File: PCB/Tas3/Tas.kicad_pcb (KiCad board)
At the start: 2 copper layers, 70 x 70 mm, 27 parts, among them J1 Shelly 1, J2 Conn_01x07, J3 USB-C, U1 MD8942, U2 Barcode, U3 CH340X, U4 ISL89410

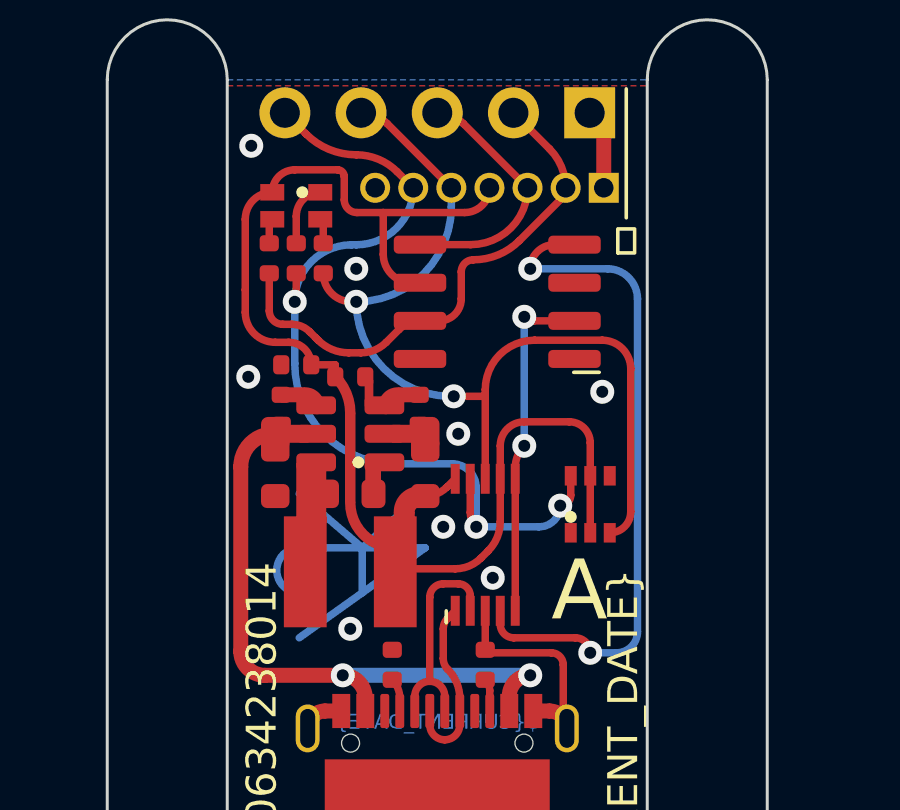
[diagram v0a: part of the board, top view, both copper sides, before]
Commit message: Fix output driver
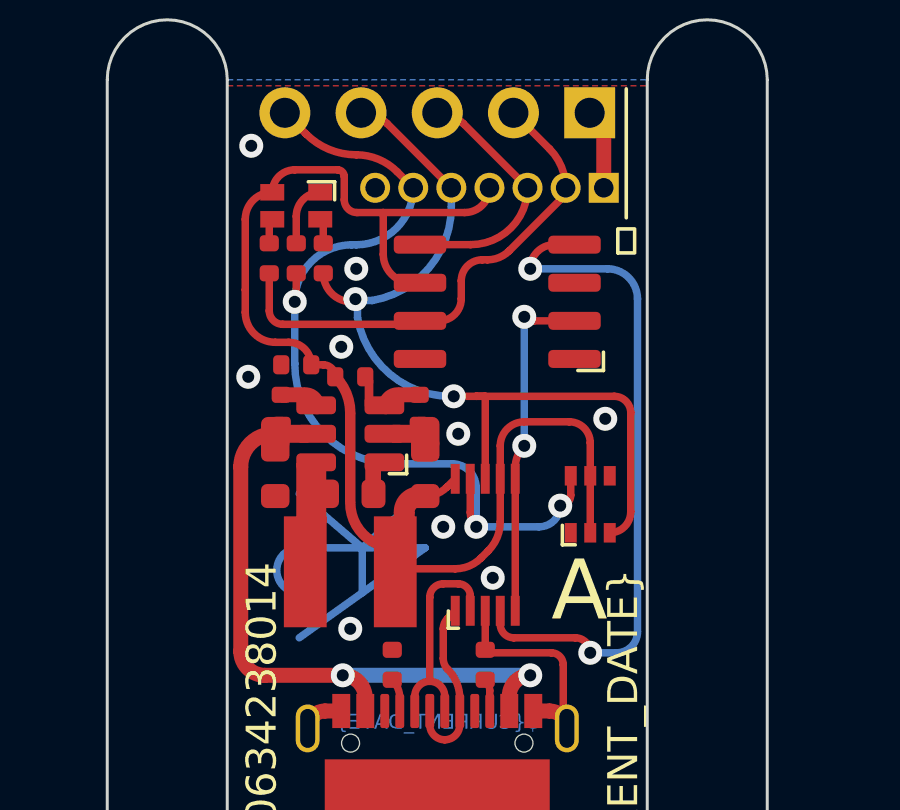
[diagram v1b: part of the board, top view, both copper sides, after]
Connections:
- U4 pad 1: unconnected-(U4-NC-Pad1) -> GND
- U4 pad 8: unconnected-(U4-NC-Pad8) -> GND
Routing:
- net G: track 32.1 -> 29.9 mm
- net B: track 17.0 -> 16.3 mm
- net GND: vias 8 -> 9

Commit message: As ordered
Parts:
- added U5: ZXGD3009E6, RevK:SOT-23-6, F.Cu at (103.4, 48.1)
- U4: value ISL89410 -> ZXGD3009E6; footprint RevK:SO-8_3.9x4.9mm_P1.27mm -> RevK:SOT-23-6
- moved U4 1.92 mm to (99.1, 48.1)
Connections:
- U4 pad 1: GND -> +3V3
- U4 pad 4: RST -> B
- U4 pad 5: RST+ -> unconnected-(U4-NC-Pad5)
- U4 pad 6: +3V3 -> B
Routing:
- net GND: track 10.8 -> 16.1 mm
- net RST+: track 8.58 -> 11.7 mm
- net +3V3: track 35.3 -> 38.2 mm
- net RST: track 22.3 -> 19.8 mm
- net B: track 16.3 -> 18.8 mm, vias 0 -> 1
- net GPIO0: track 11.2 -> 12.4 mm
- net G: track 29.9 -> 29.3 mm
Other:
- board text removed: "${TITLE}"
- board text removed: "This is an assembled printed circuit board. This is a component, with no case or leads. Snap off any extra blank panels. Use this part for your own projects as you wish. Made in China for Andrews & Arnold Ltd."
- board text removed: "®"

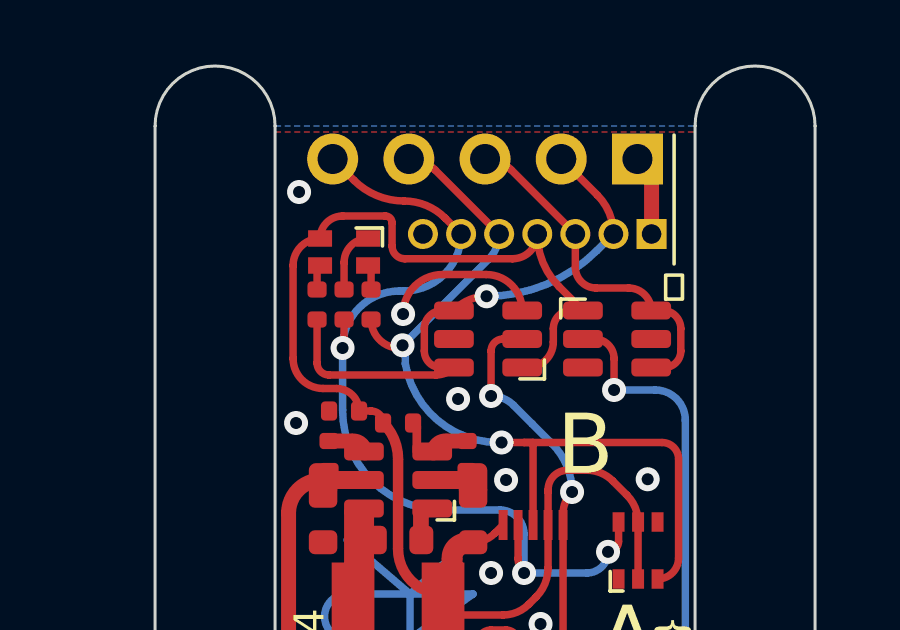
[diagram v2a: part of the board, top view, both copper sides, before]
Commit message: GPIO buffer
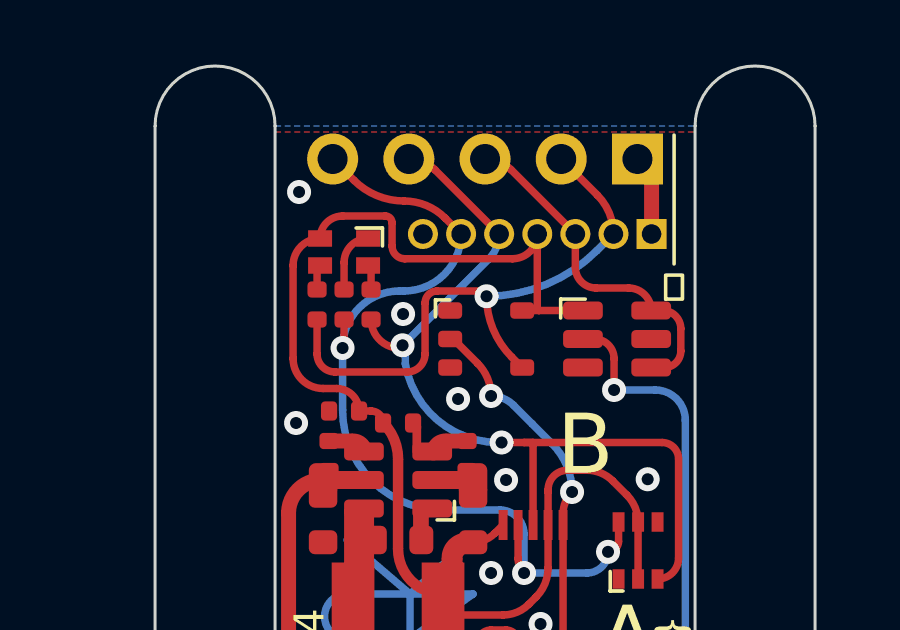
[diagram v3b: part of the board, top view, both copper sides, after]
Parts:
- removed U4: ZXGD3009E6, RevK:SOT-23-6
- added U6: 74LVC1G17W5-7, RevK:SOT-25, F.Cu at (99.0, 48.1)
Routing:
- net GND: track 16.1 -> 10.8 mm
- net +3V3: track 38.2 -> 36.5 mm
- net B: track 18.8 -> 20.1 mm

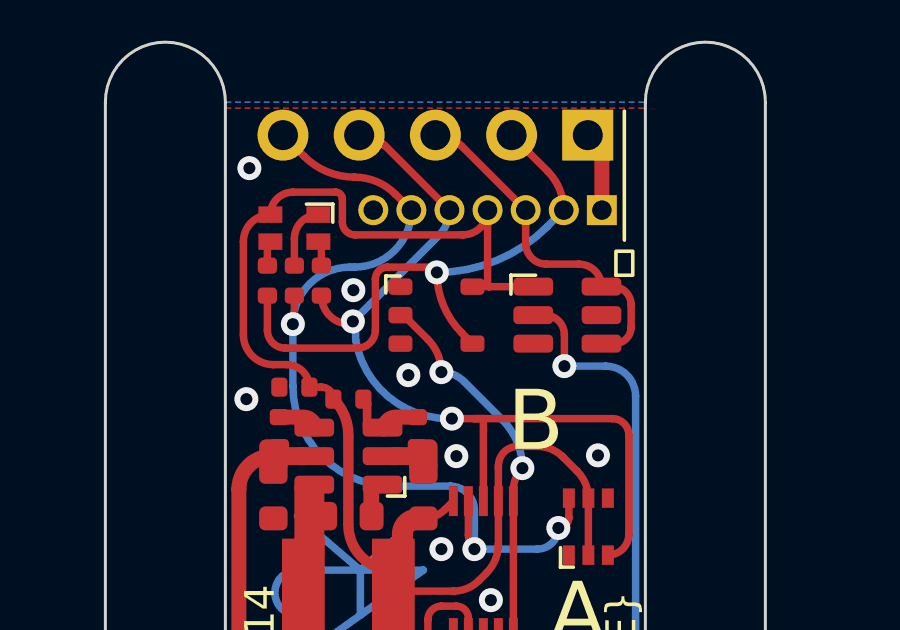
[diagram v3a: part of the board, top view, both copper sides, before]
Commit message: Put back, as does not seem to save much
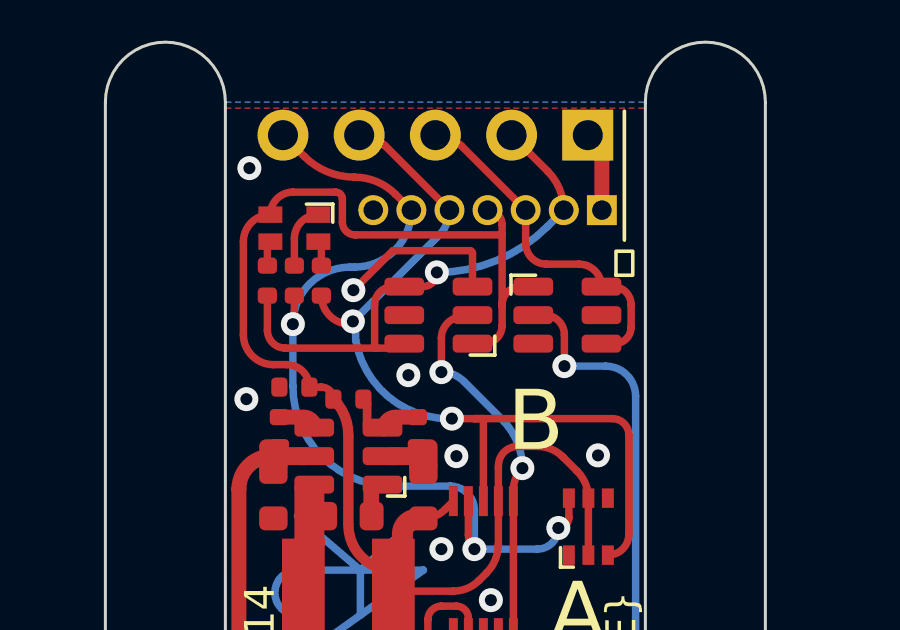
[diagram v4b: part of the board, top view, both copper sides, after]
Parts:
- removed U6: 74LVC1G17W5-7, RevK:SOT-25
- added U4: ZXGD3009E6, RevK:SOT-23-6, F.Cu at (99.1, 48.1)
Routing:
- net GND: track 10.8 -> 16.5 mm
- net B: track 20.1 -> 17.6 mm
- net +3V3: track 36.5 -> 37.9 mm
- net RST+: track 11.7 -> 10.9 mm

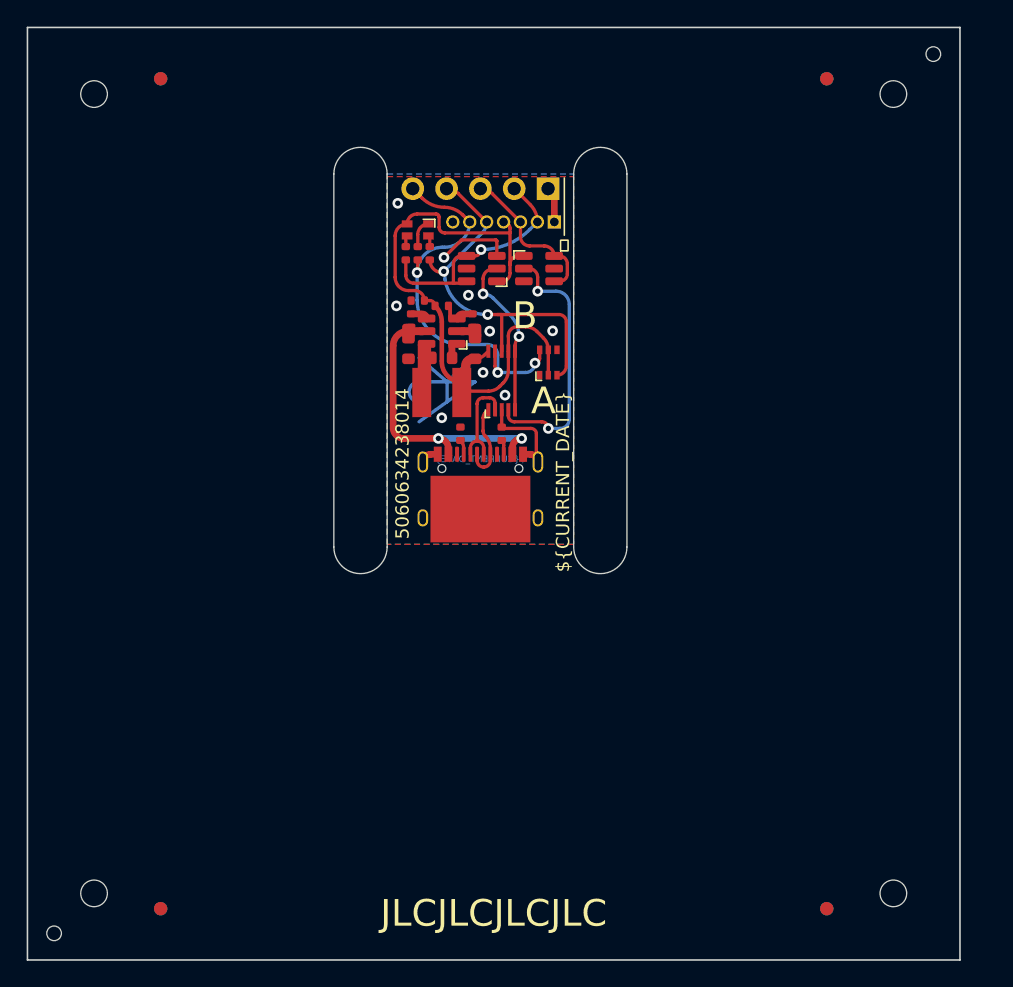
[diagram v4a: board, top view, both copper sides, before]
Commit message: Changed for cheaper assembly
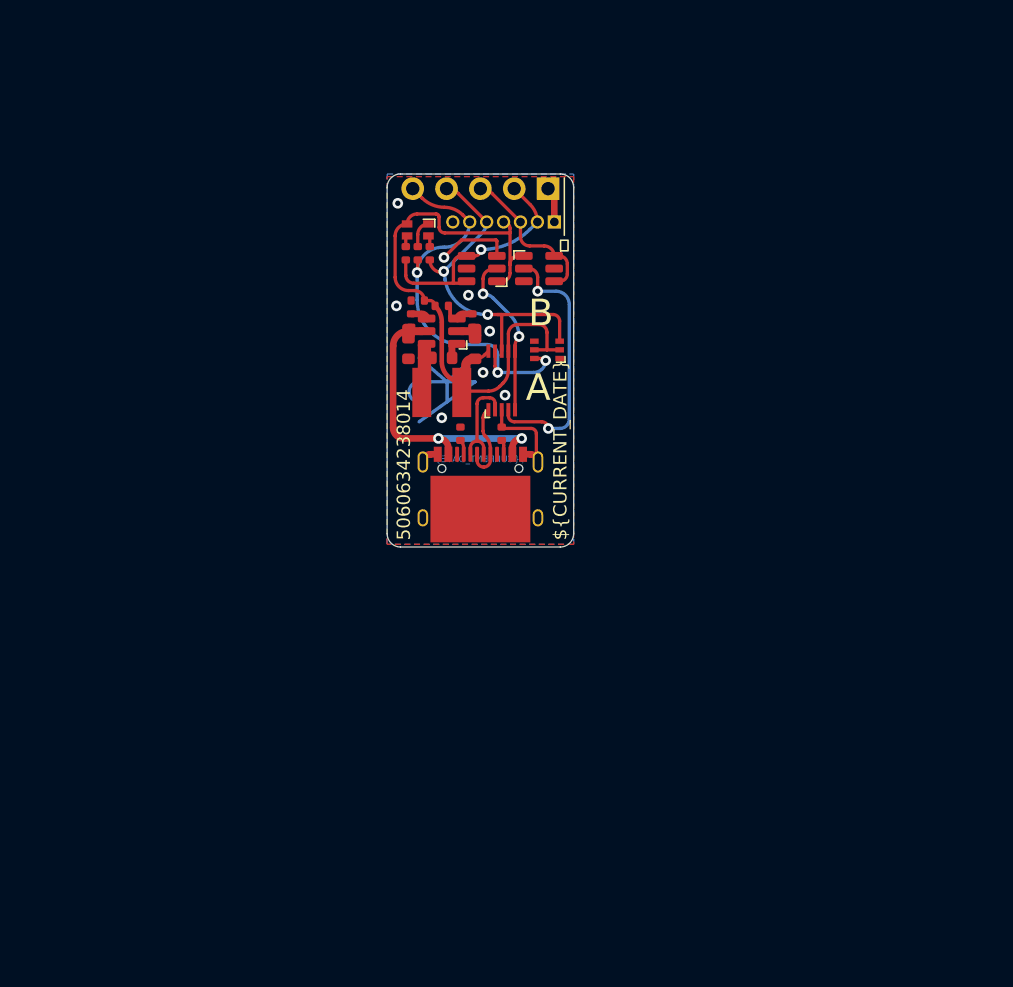
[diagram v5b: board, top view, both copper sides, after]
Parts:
- removed PCB1: 70x70, RevK:PCB7070
- removed U2: Barcode, RevK:EAN-5060634238014
- removed V1, V2: ~, RevK:VCUT70
- moved D1 0.96 mm to (104.0, 54.2), turned to 180 degrees
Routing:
- net G: track 29.3 -> 25.9 mm
- net +3V3: track 37.9 -> 38.7 mm
- net R: track 29.7 -> 30.3 mm
- net GND: vias 9 -> 8
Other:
- board size 70 x 70 mm -> 14 x 28 mm

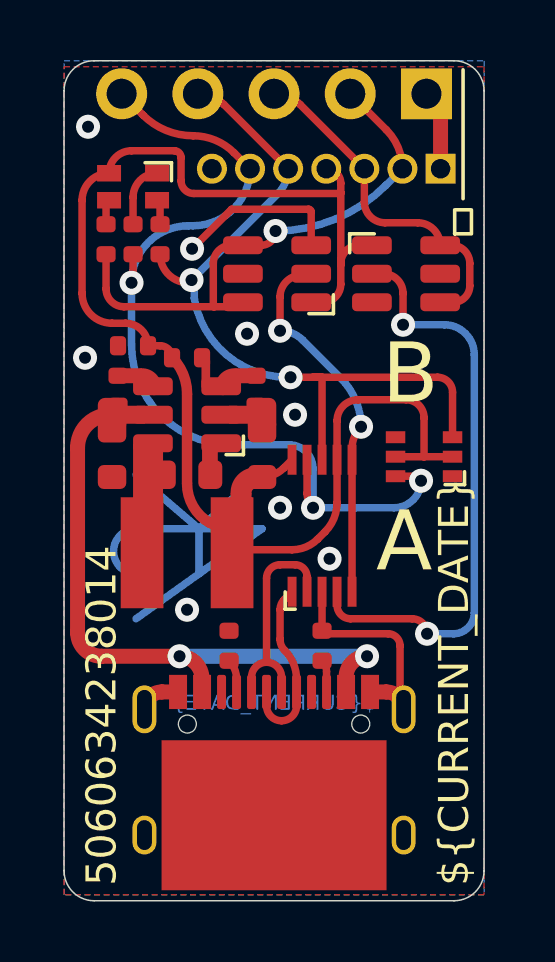
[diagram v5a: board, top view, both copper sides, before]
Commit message: Clean up pin 1 and position
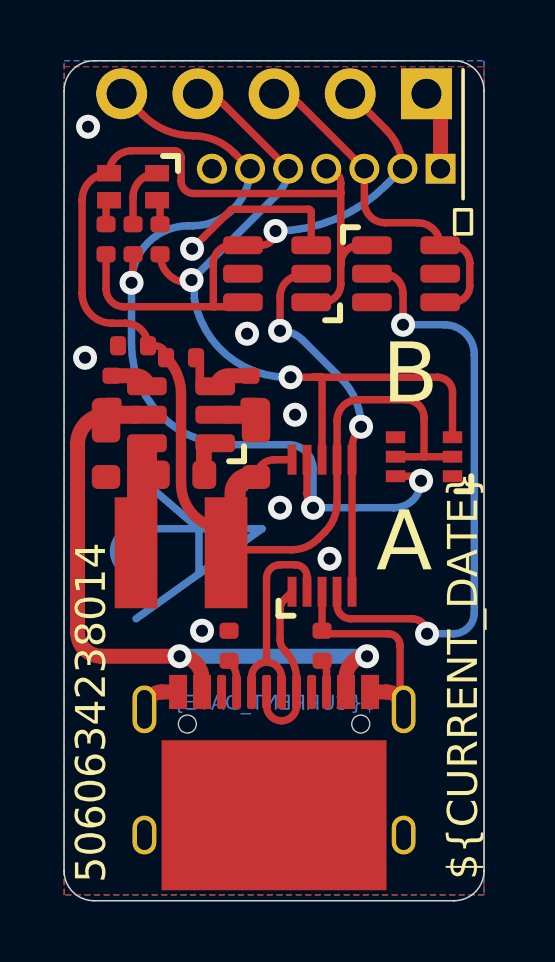
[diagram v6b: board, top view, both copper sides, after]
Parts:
- moved R10 0.20 mm to (93.6, 52.0)
- moved R4 0.20 mm to (98.2, 52.0)
- moved C1 0.20 mm to (93.4, 54.1)
- moved C6 0.20 mm to (98.4, 54.1)
- moved C7 0.20 mm to (95.9, 54.8)
- moved L2 0.20 mm to (95.9, 57.4)
- moved R3 0.20 mm to (95.9, 50.9)
- moved U1 0.20 mm to (95.9, 52.8)
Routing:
- net +3V3: track 38.7 -> 39.3 mm

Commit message: More clearance, but also the drivers dont bloody work, FFS
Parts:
- moved R4 0.20 mm to (98.4, 52.0)
- moved R10 0.20 mm to (93.4, 52.0)

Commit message: Changed voltage...
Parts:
- R4: value 40k2 -> 34k4
- moved C5 5.94 mm to (99.8, 52.8), turned to 90 degrees
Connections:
- C5 pad 1: +3V3 -> Net-(U3-V3)
- D1 pad 2: +3V3 -> +3V8
- D1 pad 5: +3V3 -> +3V8
- D5 pad 4: +3V3 -> +3V8
- J2 pad 4: +3V3 -> RST+
- U1 pad 8: +3V3 -> +3V8
- U3 pad 10: +3V3 -> Net-(U3-V3)
- U3 pad 7: +3V3 -> VBUS
- U4 pad 1: +3V3 -> +3V8
- U5 pad 1: +3V3 -> +3V8
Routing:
- net +3V3: track 39.3 -> 0.00 mm
- net +3V8: track 0.00 -> 32.2 mm
- net VBUS: track 21.0 -> 34.8 mm, vias 2 -> 3
- net GND: track 16.5 -> 28.4 mm
- net RST+: track 10.9 -> 12.2 mm
- net Net-(U3-V3): track 0.00 -> 1.10 mm
- net GPIO0: track 11.8 -> 12.4 mm
